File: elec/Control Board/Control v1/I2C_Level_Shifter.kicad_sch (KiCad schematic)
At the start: 0 parts

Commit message: Add Lees PublicInvention submodule library. Update Control V1 project and schematic for new library.
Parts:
- added C201, C202: 1uF, Capacitor_SMD:C_0603_1608Metric_Pad1.08x0.95mm_HandSolder, symbol Device:C
- added C203, C204: 39PF, Capacitor_SMD:C_0603_1608Metric_Pad1.08x0.95mm_HandSolder, symbol Device:C
- added J201: 0.100_2Pin, Connector_PinHeader_2.54mm:PinHeader_1x02_P2.54mm_Vertical, symbol GPAD_SCH_LIB:22-23-2021
- added J202: Conn_01x04, Connector_PinHeader_2.54mm:PinHeader_1x04_P2.54mm_Vertical, symbol Connector_Generic:Conn_01x04
- added Q201, Q202: BSS138, Package_TO_SOT_SMD:SOT-23, symbol Transistor_FET:BSS138
- added R201, R208: 1R, Resistor_SMD:R_0603_1608Metric_Pad0.98x0.95mm_HandSolder, symbol Device:R
- added R202, R203, R204, R205: 10K, Resistor_SMD:R_0603_1608Metric_Pad0.98x0.95mm_HandSolder, symbol Device:R
- added R206, R207: 39R, Resistor_SMD:R_0603_1608Metric_Pad0.98x0.95mm_HandSolder, symbol Device:R
- added R209, R210: DNI, Resistor_SMD:R_0603_1608Metric_Pad0.98x0.95mm_HandSolder, symbol Device:R
- added TP201: I2C_VCC, TestPoint:TestPoint_Loop_D2.54mm_Drill1.5mm_Beaded, symbol Connector:TestPoint
- added TP202: SCL_5V, TestPoint:TestPoint_Loop_D2.54mm_Drill1.5mm_Beaded, symbol Connector:TestPoint
- added TP203: SDA_5V, TestPoint:TestPoint_Loop_D2.54mm_Drill1.5mm_Beaded, symbol Connector:TestPoint
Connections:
- new net: Q202.3 (D), R205.2, R207.2
- new net: Q201.3 (D), R204.2, R206.2
- new net +12forSPIPeripherial: J201.2, R210.2
- new net +3V3LevelShift: R201.1
- new net +3V3Local: C201.1, Q201.1 (G), Q202.1 (G), R201.2, R202.1, R203.1
- new net +5LevelShift: R208.2, R209.2
- new net +5VLocal: C202.1, R204.1, R205.1, R208.1
- new net GND: C201.2, C202.2, C203.2, C204.2, J202.3 (Pin_3)
- new net I2C_VCC: J201.1, J202.1 (Pin_1), R209.1, R210.1, TP201.1
- new net SCL_3.3V: Q201.2 (S), R202.2
- new net SCL_5V: C203.1, J202.2 (Pin_2), R206.1, TP202.1
- new net SDA_3.3V: Q202.2 (S), R203.2
- new net SDA_5V: C204.1, J202.4 (Pin_4), R207.1, TP203.1
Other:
- note added: "Bring out I2C bus through bidirectional level shifters."
- note added: "I2C Connector Signal Names"
- note added: "Power to I2C interface, 5V or 12V."
- note added: "SCL_5V: Serial Clock at 5V SDA_5V: Serial Data at 5V"

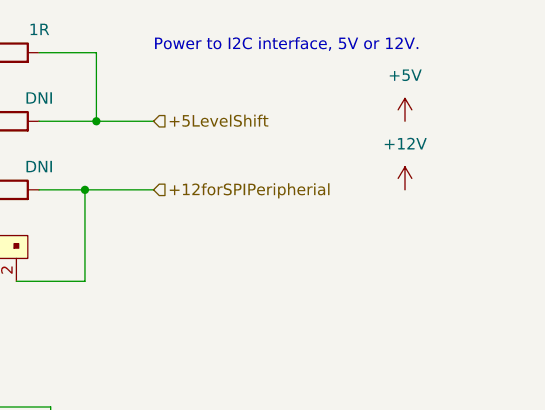
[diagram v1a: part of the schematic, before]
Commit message: Move some components for rough placement.
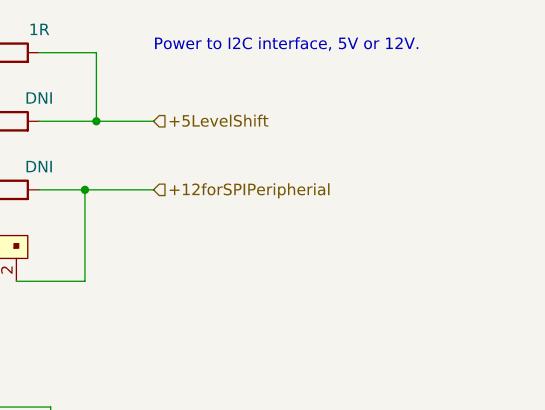
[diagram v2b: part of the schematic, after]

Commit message: Fix swome ERC errors.
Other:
- moved on the sheet: C201, C202, C203, C204, J201, J202, Q201, Q202, R201, R202, R203, R204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

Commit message: Net name congruancy.
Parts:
- J202: AssemblyType (none) -> HAND
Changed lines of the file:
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@@
       (project "Control v1"
         (path "/c68c9deb-8d4d-42f0-adf8-4d3022f4ee59/905a527a-e45b-4998-adf0-069f9c917f28"
-          (reference "TP17") (unit 1)
+          (reference "TP21") (unit 1)
         )
       )
@@
       (project "Control v1"
         (path "/c68c9deb-8d4d-42f0-adf8-4d3022f4ee59/905a527a-e45b-4998-adf0-069f9c917f28"
-          (reference "#PWR070") (unit 1)
+          (reference "#PWR069") (unit 1)
         )
       )
@@
       (project "Control v1"
         (path "/c68c9deb-8d4d-42f0-adf8-4d3022f4ee59/905a527a-e45b-4998-adf0-069f9c917f28"
-          (reference "TP16") (unit 1)
+          (reference "TP20") (unit 1)
         )
       )
@@
       (effects (font (size 1.27 1.27)) hide)
     )
+    (property "AssemblyType" "HAND" (at 228.6 95.25 0)
+      (effects (font (size 1.27 1.27)) hide)
+    )
     (pin "1")
     (pin "2")
@@
       (project "Control v1"
         (path "/c68c9deb-8d4d-42f0-adf8-4d3022f4ee59/905a527a-e45b-4998-adf0-069f9c917f28"
-          (reference "TP15") (unit 1)
+          (reference "TP19") (unit 1)
         )
       )
@@
     )
   )
-  (symbol (lib_id "power:GND") (at 199.39 102.87 0) (unit 1)
+  (symbol (lib_name "GND_2") (lib_id "power:GND") (at 199.39 102.87 0) (unit 1)
     (in_bom yes) (on_board yes) (dnp no)
     (property "Reference" "#PWR0203" (at 199.39 109.22 0)
@@
       (project "Control v1"
         (path "/c68c9deb-8d4d-42f0-adf8-4d3022f4ee59/905a527a-e45b-4998-adf0-069f9c917f28"
-          (reference "#PWR068") (unit 1)
-        )
-      )
-    )
-  )
-  (symbol (lib_id "power:GND") (at 148.59 38.1 0) (unit 1)
+          (reference "#PWR067") (unit 1)
+        )
+      )
+    )
+  )
+  (symbol (lib_name "GND_4") (lib_id "power:GND") (at 148.59 38.1 0) (unit 1)
     (in_bom yes) (on_board yes) (dnp no) (fields_autoplaced)
     (property "Reference" "#PWR0202" (at 148.59 44.45 0)
@@
       (project "Control v1"
         (path "/c68c9deb-8d4d-42f0-adf8-4d3022f4ee59/905a527a-e45b-4998-adf0-069f9c917f28"
-          (reference "#PWR067") (unit 1)
+          (reference "#PWR066") (unit 1)
         )
       )
@@
     )
   )
-  (symbol (lib_id "power:GND") (at 205.74 113.03 0) (unit 1)
+  (symbol (lib_name "GND_1") (lib_id "power:GND") (at 205.74 113.03 0) (unit 1)
     (in_bom yes) (on_board yes) (dnp no)
     (property "Reference" "#PWR0204" (at 205.74 119.38 0)
@@
       (project "Control v1"
         (path "/c68c9deb-8d4d-42f0-adf8-4d3022f4ee59/905a527a-e45b-4998-adf0-069f9c917f28"
-          (reference "#PWR069") (unit 1)
+          (reference "#PWR068") (unit 1)
         )
       )
@@
     )
   )
-  (symbol (lib_id "power:GND") (at 104.14 57.15 0) (unit 1)
+  (symbol (lib_name "GND_3") (lib_id "power:GND") (at 104.14 57.15 0) (unit 1)
     (in_bom yes) (on_board yes) (dnp no) (fields_autoplaced)
     (property "Reference" "#PWR0201" (at 104.14 63.5 0)
@@
       (project "Control v1"
         (path "/c68c9deb-8d4d-42f0-adf8-4d3022f4ee59/905a527a-e45b-4998-adf0-069f9c917f28"
-          (reference "#PWR066") (unit 1)
-        )
-      )
+          (reference "#PWR065") (unit 1)
+        )
+      )
